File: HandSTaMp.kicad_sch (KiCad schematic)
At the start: 18 parts, among them J1 USB_C_Receptacle_USB2.0_16P, J2 SWD, J3 Pins, SW0 BOOT, SW1 Row 0, Col+0, SW2 Row 0, Col+1, U2 PRTR5V0U2X, U4 CH32X035G8U6

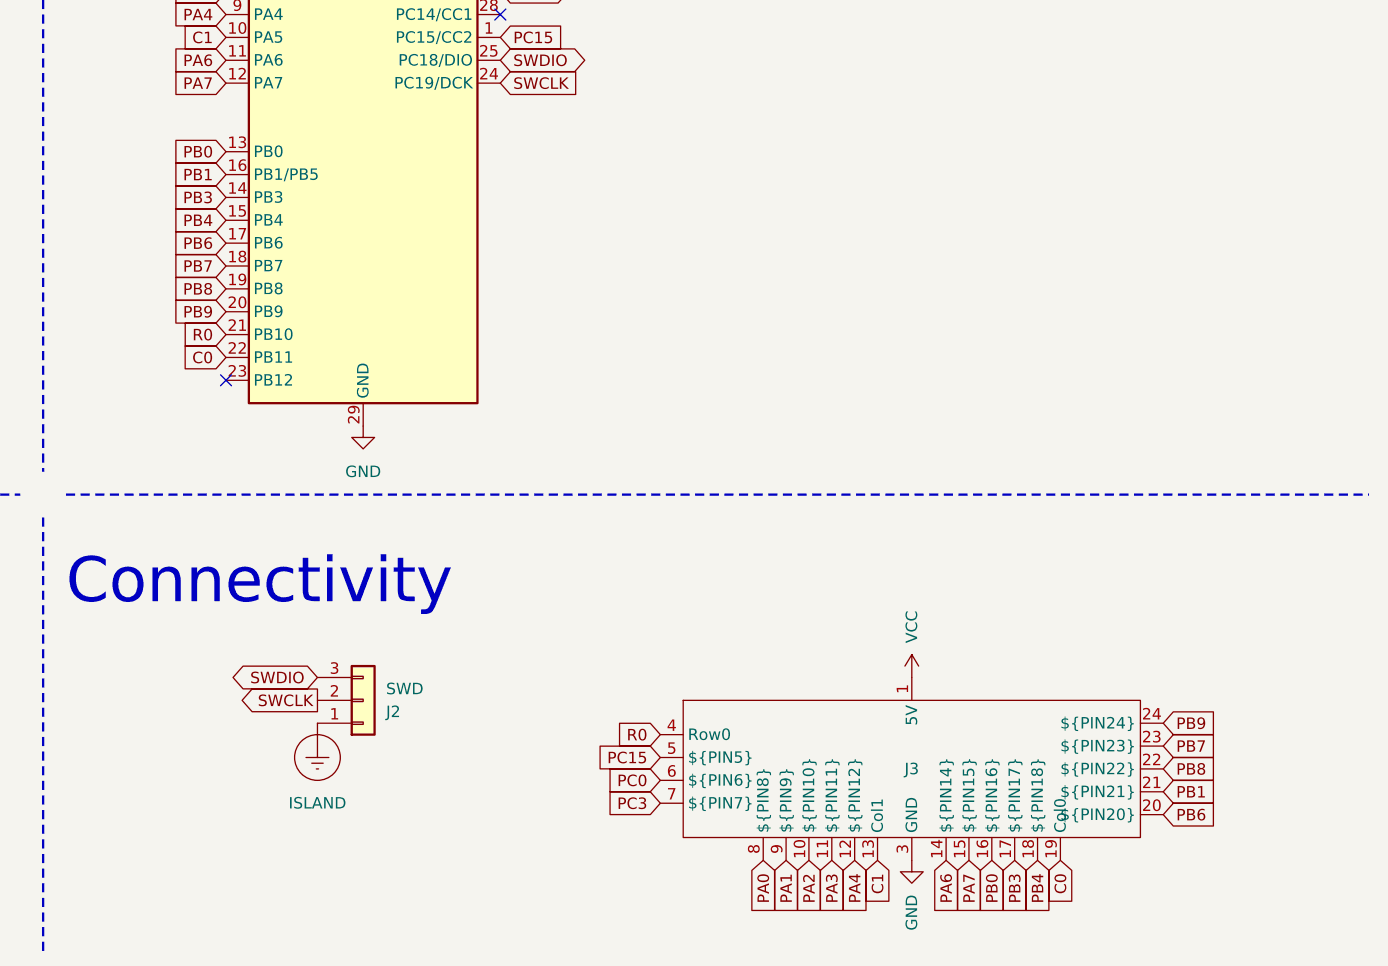
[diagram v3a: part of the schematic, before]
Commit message: Fix pin 16
This can PB1 or PB5, but the latter is the default.
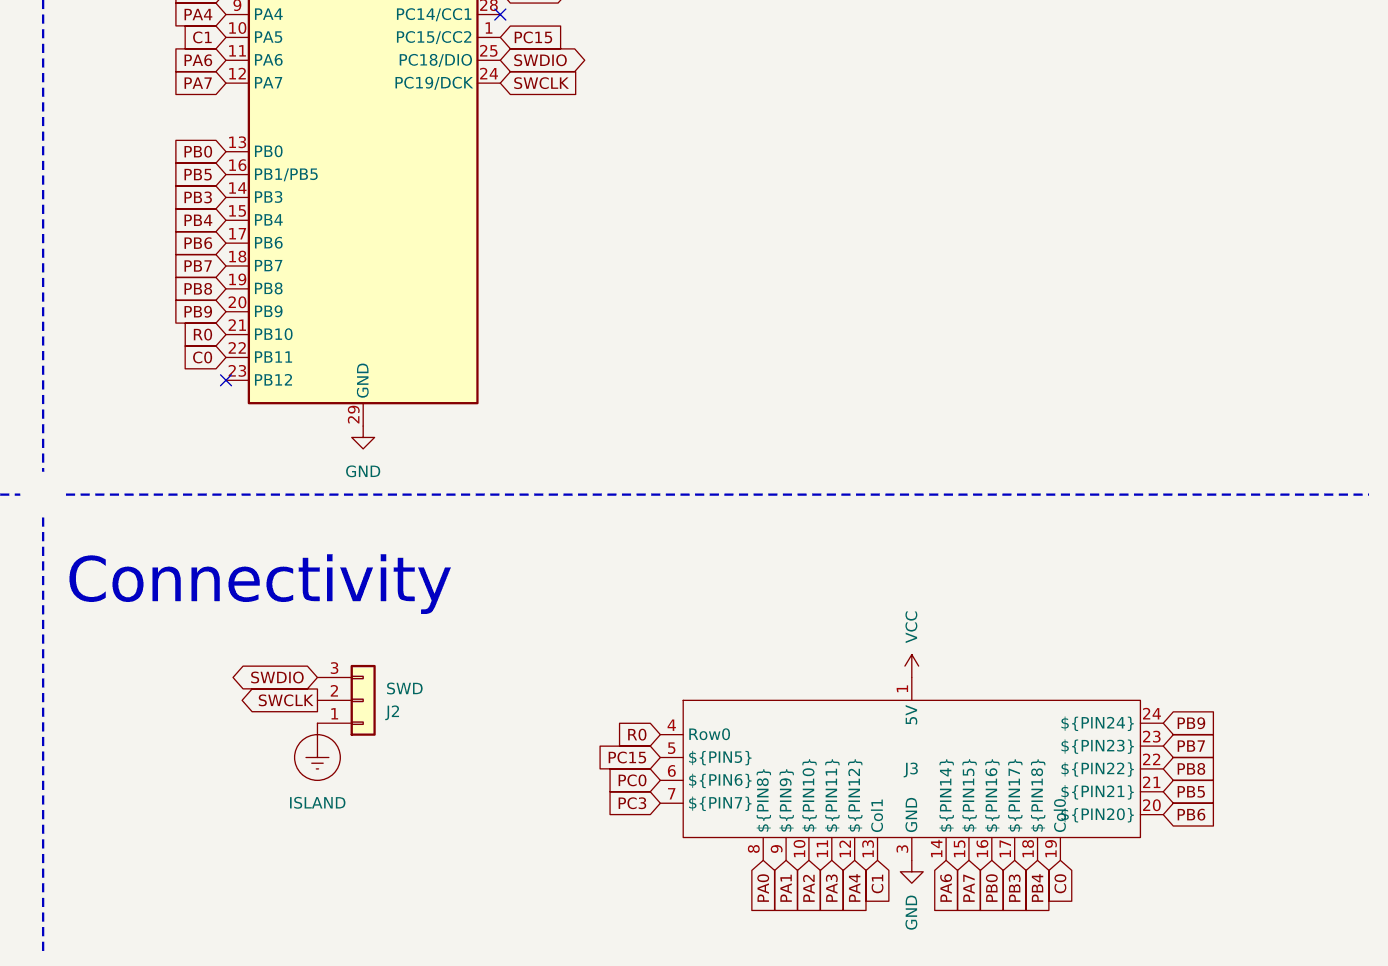
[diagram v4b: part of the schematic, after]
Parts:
- J3: PIN21 B1 -> B5
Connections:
- net PB1 renamed PB5
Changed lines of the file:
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@@
 		)
 	)
-	(global_label "PB1"
+	(global_label "PB5"
 		(shape input)
 		(at 154.94 73.66 180)
@@
 		)
 		(property "Intersheetrefs" "${INTERSHEET_REFS}"
-			(at 149.2391 73.66 0)
+			(at 149.1138 73.66 0)
 			(hide yes)
 			(show_name no)
@@
 		)
 	)
-	(global_label "PB1"
+	(global_label "PB5"
 		(shape input)
 		(at 259.08 142.24 0)
@@
 		)
 		(property "Intersheetrefs" "${INTERSHEET_REFS}"
-			(at 264.7809 142.24 0)
+			(at 264.9062 142.24 0)
 			(hide yes)
 			(show_name no)
@@
 			)
 		)
-		(property "PIN21" "B1"
+		(property "PIN21" "B5"
 			(at 231.14 139.7 0)
 			(hide yes)

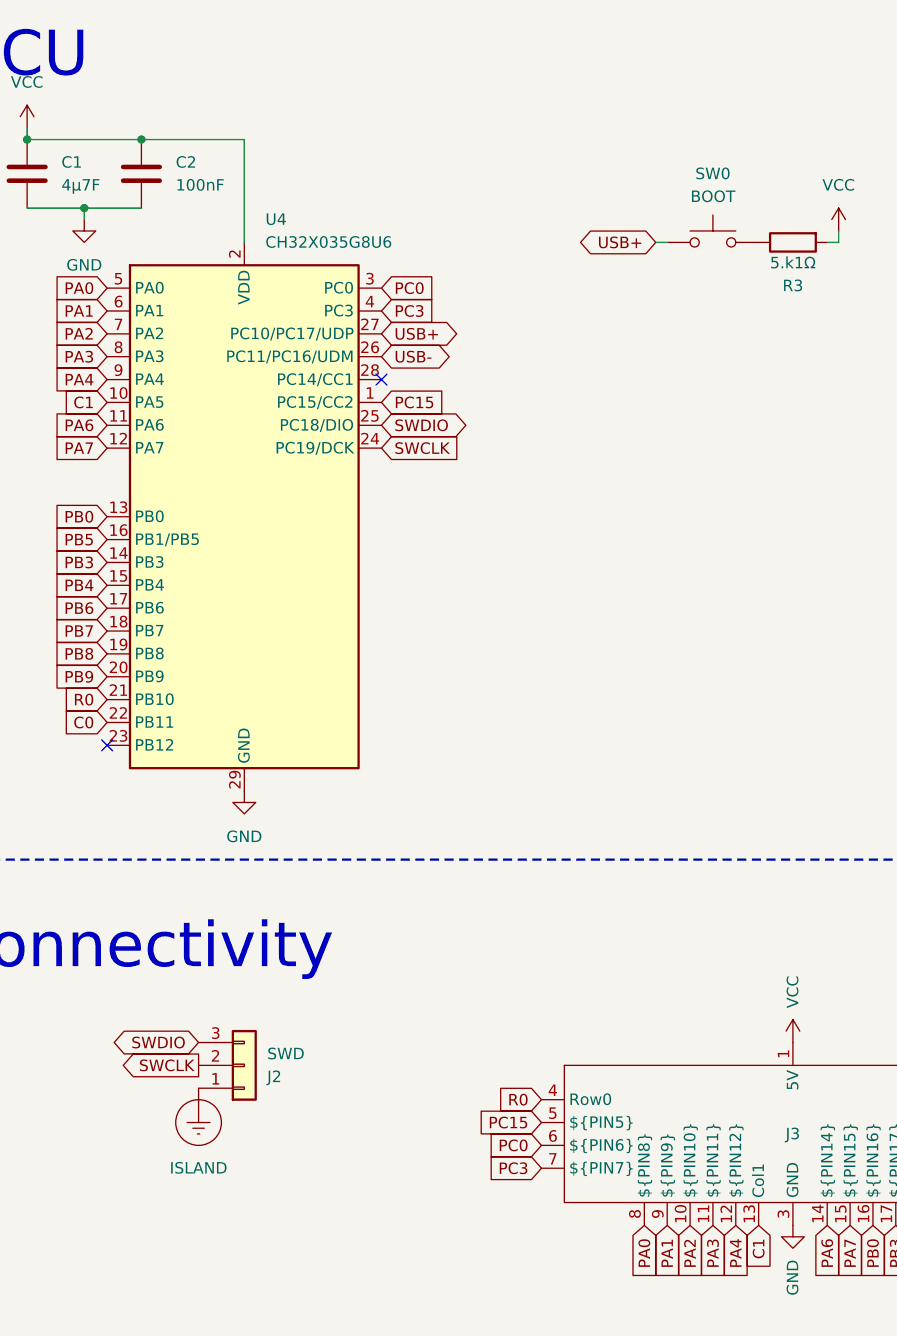
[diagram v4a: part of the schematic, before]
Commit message: Update SWD/SDI and Shield connections
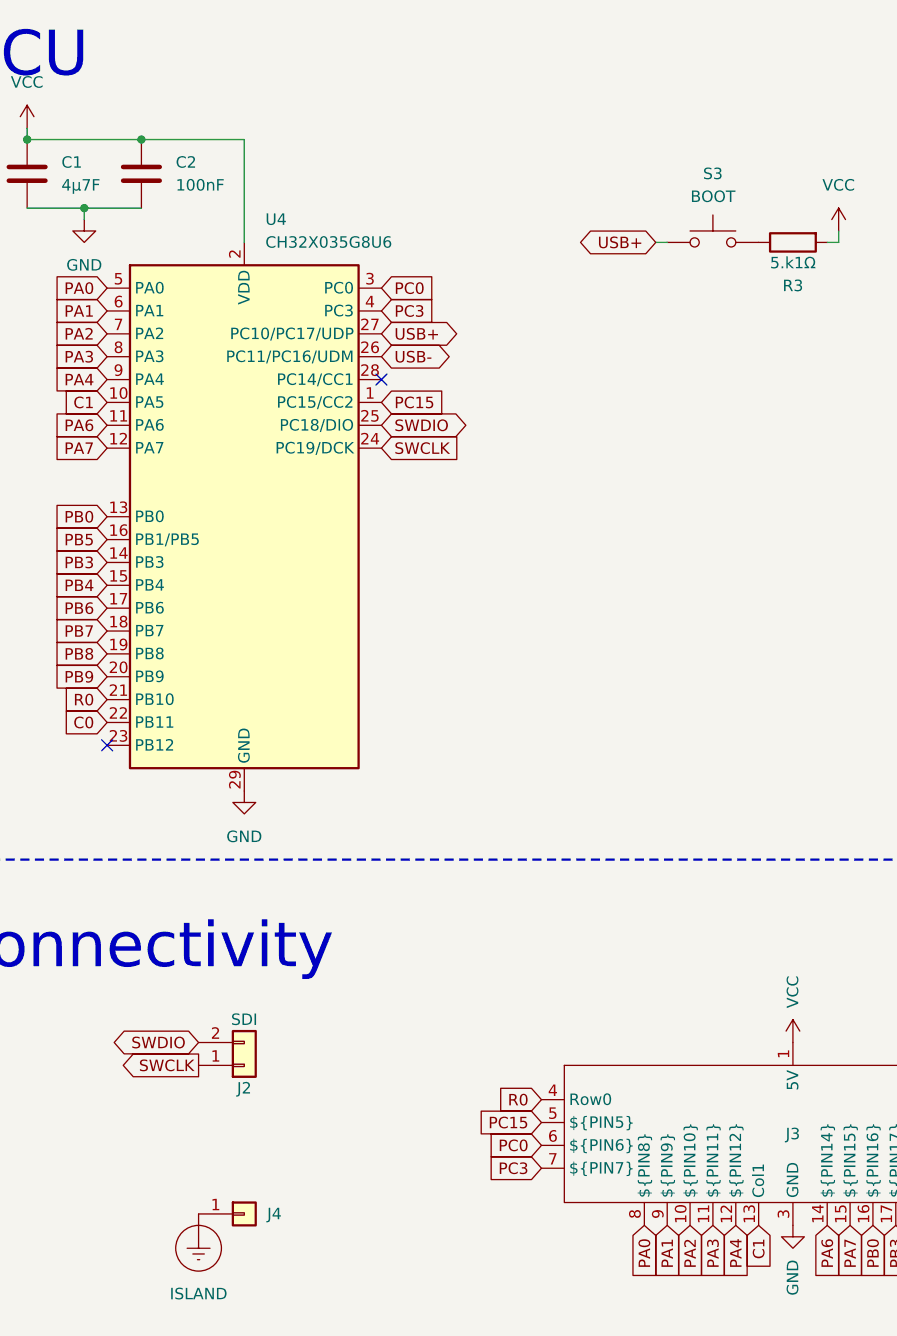
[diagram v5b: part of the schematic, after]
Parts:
- added J4: ⏚, Project Library:SolderWire_1x01_D1mm_OD1.7mm, symbol Connector_Generic:Conn_01x01
- J2: value SWD -> SDI; footprint Project Library:SWD+GroundingPoint -> Project Library:SWD; symbol Connector_Generic:Conn_01x03 -> Connector_Generic:Conn_01x02
- renumbered SW0 to S3
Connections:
- net ISLAND: now also J4.1 (Pin_1); no longer J2.1 (Pin_1)
- net SWCLK: now also J2.1 (Pin_1); no longer J2.2 (Pin_2)
- net SWDIO: now also J2.2 (Pin_2); no longer J2.3 (Pin_3)
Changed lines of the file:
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@@
+	)
+	(symbol
+		(lib_id "power:Earth_Protective")
+		(at 165.1 148.59 0)
+		(unit 1)
+		(body_style 1)
+		(exclude_from_sim no)
+		(in_bom yes)
+		(on_board yes)
+		(in_pos_files yes)
+		(dnp no)
+		(fields_autoplaced yes)
+		(property "Reference" "#PWR033"
+			(at 165.1 158.75 0)
+			(hide yes)
+			(show_name no)
+			(do_not_autoplace no)
+			(effects
+				(font
+					(size 1.27 1.27)
+				)
+			)
+		)
+		(property "Value" "ISLAND"
+			(at 165.1 157.48 0)
+			(show_name no)
+			(do_not_autoplace no)
+			(effects
+				(font
+					(size 1.27 1.27)
+				)
+			)
+		)
+		(property "Footprint" ""
+			(at 165.1 151.13 0)
+			(hide yes)
+			(show_name no)
+			(do_not_autoplace no)
+			(effects
+				(font
+					(size 1.27 1.27)
+				)
+			)
+		)
+		(property "Datasheet" ""
+			(at 165.1 151.13 0)
+			(hide yes)
+			(show_name no)
+			(do_not_autoplace no)
+			(effects
+				(font
+					(size 1.27 1.27)
+				)
+			)
+		)
+		(property "Description" "Power symbol creates a global label with name \"Earth_Protective\""
+			(at 165.1 148.59 0)
+			(hide yes)
+			(show_name no)
+			(do_not_autoplace no)
+			(effects
+				(font
+					(size 1.27 1.27)
+				)
+			)
+		)
+		(pin "1"
+		)
+		(instances
+			(project "HandSTaMp"
+				(path "/34400e51-cf83-464a-b3ec-e9a28a972a27"
+					(reference "#PWR033")
+					(unit 1)
+				)
+			)
+		)
 	)
 	(symbol
@@
 	)
 	(symbol
-		(lib_id "Connector_Generic:Conn_01x03")
+		(lib_id "Connector_Generic:Conn_01x02")
 		(at 170.18 132.08 0)
 		(mirror x)
@@
 		(dnp no)
 		(property "Reference" "J2"
-			(at 172.72 133.35 0)
-			(show_name no)
-			(do_not_autoplace no)
-			(effects
-				(font
-					(size 1.27 1.27)
-				)
-				(justify left)
-			)
-		)
-		(property "Value" "SWD"
-			(at 172.72 130.81 0)
-			(show_name no)
-			(do_not_autoplace no)
-			(effects
-				(font
-					(size 1.27 1.27)
-				)
-				(justify left)
-			)
-		)
-		(property "Footprint" "Project Library:SWD+GroundingPoint"
+			(at 170.18 134.62 0)
+			(show_name no)
+			(do_not_autoplace no)
+			(effects
+				(font
+					(size 1.27 1.27)
+				)
+			)
+		)
+		(property "Value" "SDI"
+			(at 170.18 127 0)
+			(show_name no)
+			(do_not_autoplace no)
+			(effects
+				(font
+					(size 1.27 1.27)
+				)
+			)
+		)
+		(property "Footprint" "Project Library:SWD"
 			(at 170.18 132.08 0)
 			(hide yes)
@@
 			)
 		)
-		(property "Description" "Generic connector, single row, 01x03, script generated (kicad-library-utils/schlib/autogen/connector/)"
+		(property "Description" "Generic connector, single row, 01x02, script generated (kicad-library-utils/schlib/autogen/connector/)"
 			(at 170.18 132.08 0)
 			(hide yes)
@@
 		)
 		(pin "2"
-		)
-		(pin "3"
 		)
 		(instances
@@
 		(dnp no)
 		(fields_autoplaced yes)
-		(property "Reference" "SW0"
+		(property "Reference" "S3"
 			(at 222.25 33.02 0)
 			(show_name no)
@@
 			(project "HandSTaMp"
 				(path "/34400e51-cf83-464a-b3ec-e9a28a972a27"
-					(reference "SW0")
+					(reference "S3")
 					(unit 1)
 				)
@@
 	)
 	(symbol
+		(lib_id "Connector_Generic:Conn_01x01")
+		(at 170.18 148.59 0)
+		(unit 1)
+		(body_style 1)
+		(exclude_from_sim no)
+		(in_bom yes)
+		(on_board yes)
+		(in_pos_files yes)
+		(dnp no)
+		(fields_autoplaced yes)
+		(property "Reference" "J4"
+			(at 172.72 148.59 0)
+			(show_name no)
+			(do_not_autoplace no)
+			(effects
+				(font
+					(size 1.27 1.27)
+				)
+				(justify left)
+			)
+		)
+		(property "Value" "⏚"
+			(at 172.72 149.86 0)
+			(hide yes)
+			(show_name no)
+			(do_not_autoplace no)
+			(effects
+				(font
+					(size 1.27 1.27)
+				)
+				(justify left)
+			)
+		)
+		(property "Footprint" "Project Library:SolderWire_1x01_D1mm_OD1.7mm"
+			(at 170.18 148.59 0)
+			(hide yes)
+			(show_name no)
+			(do_not_autoplace no)
+			(effects
+				(font
+					(size 1.27 1.27)
+				)
+			)
+		)
+		(property "Datasheet" ""
+			(at 170.18 148.59 0)
+			(hide yes)
+			(show_name no)
+			(do_not_autoplace no)
+			(effects
+				(font
+					(size 1.27 1.27)
+				)
+			)
+		)
+		(property "Description" "Generic connector, single row, 01x01, script generated (kicad-library-utils/schlib/autogen/connector/)"
+			(at 170.18 148.59 0)
+			(hide yes)
+			(show_name no)
+			(do_not_autoplace no)
+			(effects
+				(font
+					(size 1.27 1.27)
+				)
+			)
+		)
+		(pin "1"
+		)
+		(instances
+			(project "HandSTaMp"
+				(path "/34400e51-cf83-464a-b3ec-e9a28a972a27"
+					(reference "J4")
+					(unit 1)
+				)
+			)
+		)
+	)
+	(symbol
 		(lib_id "power:VCC")
 		(at 119.38 35.56 270)
@@
 					(unit 1)
 				)
-			)
-		)
-	)
-	(symbol
-		(lib_id "power:Earth_Protective")
-		(at 165.1 134.62 0)
-		(unit 1)
-		(body_style 1)
-		(exclude_from_sim no)
-		(in_bom yes)
-		(on_board yes)
-		(in_pos_files yes)
-		(dnp no)
-		(fields_autoplaced yes)
-		(property "Reference" "#PWR032"
-			(at 165.1 144.78 0)
-			(hide yes)
-			(show_name no)
-			(do_not_autoplace no)
-			(effects
-				(font
-					(size 1.27 1.27)
-				)
-			)
-		)
-		(property "Value" "ISLAND"
-			(at 165.1 143.51 0)
-			(show_name no)
-			(do_not_autoplace no)
-			(effects
-				(font
-					(size 1.27 1.27)
-				)
-			)
-		)
-		(property "Footprint" ""
-			(at 165.1 137.16 0)
-			(hide yes)
-			(show_name no)
-			(do_not_autoplace no)
-			(effects
-				(font
-					(size 1.27 1.27)
-				)
-			)
-		)
-		(property "Datasheet" ""
-			(at 165.1 137.16 0)
-			(hide yes)
-			(show_name no)
-			(do_not_autoplace no)
-			(effects
-				(font
-					(size 1.27 1.27)
-				)
-			)
-		)
-		(property "Description" "Power symbol creates a global label with name \"Earth_Protective\""
-			(at 165.1 134.62 0)
-			(hide yes)
-			(show_name no)
-			(do_not_autoplace no)
-			(effects
-				(font
-					(size 1.27 1.27)
-				)
-			)
-		)
-		(pin "1"
-		)
-		(instances
-			(project "HandSTaMp"
-				(path "/34400e51-cf83-464a-b3ec-e9a28a972a27"
-					(reference "#PWR032")
-					(unit 1)
-				)

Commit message: Add one alignment pin hole to each MX switch
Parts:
- SW1: footprint Project Library:SW_MX_1u_PlateMount -> Project Library:SW_MX_1u_1pinL
- SW2: footprint Project Library:SW_MX_1u_PlateMount -> Project Library:SW_MX_1u_1pinR
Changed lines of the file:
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@@
 			)
 		)
-		(property "Footprint" "Project Library:SW_MX_1u_PlateMount"
+		(property "Footprint" "Project Library:SW_MX_1u_1pinR"
 			(at 116.84 129.54 0)
 			(hide yes)
@@
 			)
 		)
-		(property "Footprint" "Project Library:SW_MX_1u_PlateMount"
+		(property "Footprint" "Project Library:SW_MX_1u_1pinL"
 			(at 91.44 129.54 0)
 			(hide yes)
